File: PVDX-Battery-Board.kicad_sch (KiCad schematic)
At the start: 0 parts

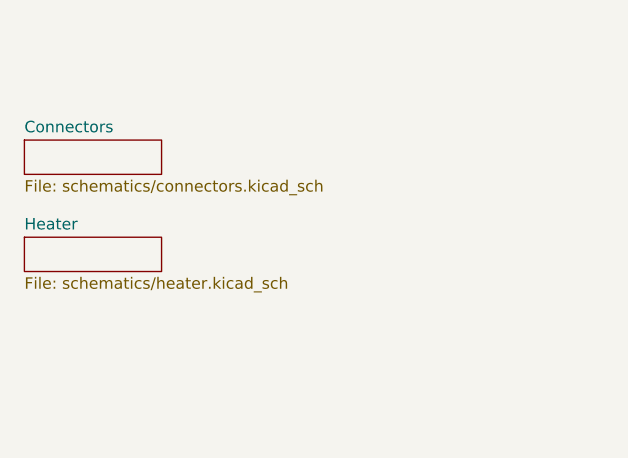
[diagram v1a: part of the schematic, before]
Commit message: Add battery overdischarge & short protections to board
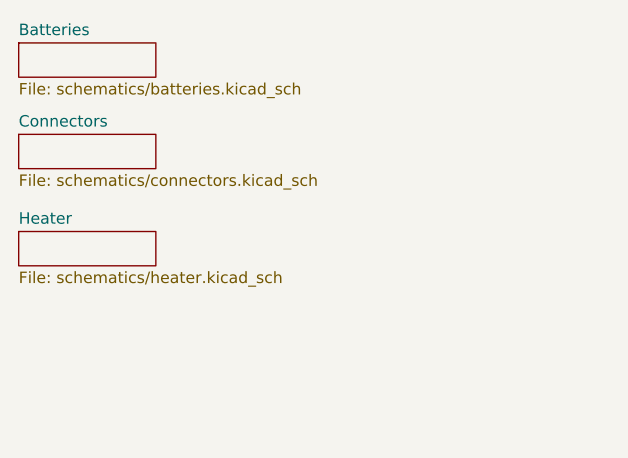
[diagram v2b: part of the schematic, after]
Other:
- added sheet Batteries (schematics/batteries.kicad_sch)
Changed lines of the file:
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@@
 	)
 	(sheet
-		(at 47.625 58.42)
+		(at 46.99 36.83)
+		(size 15.24 3.81)
+		(exclude_from_sim no)
+		(in_bom yes)
+		(on_board yes)
+		(dnp no)
+		(fields_autoplaced yes)
+		(stroke
+			(width 0.1524)
+			(type solid)
+		)
+		(fill
+			(color 0 0 0 0)
+		)
+		(property "Sheetname" "Batteries"
+			(at 46.99 36.1184 0)
+			(show_name no)
+			(do_not_autoplace no)
+			(effects
+				(font
+					(size 1.27 1.27)
+				)
+				(justify left bottom)
+			)
+		)
+		(property "Sheetfile" "schematics/batteries.kicad_sch"
+			(at 46.99 41.2246 0)
+			(show_name no)
+			(do_not_autoplace no)
+			(effects
+				(font
+					(size 1.27 1.27)
+				)
+				(justify left top)
+			)
+		)
+		(instances
+			(project "PVDX-Battery-Board"
+				(path "/c318761a-e6d3-4e59-aaa2-0d170bce7cde"
+					(page "4")
+				)
+			)
+		)
+	)
+	(sheet
+		(at 46.99 57.785)
 		(size 15.24 3.81)
 		(exclude_from_sim no)
@@
 		)
 		(property "Sheetname" "Heater"
-			(at 47.625 57.7084 0)
+			(at 46.99 57.0734 0)
 			(show_name no)
 			(do_not_autoplace no)
@@
 		)
 		(property "Sheetfile" "schematics/heater.kicad_sch"
-			(at 47.625 62.8146 0)
+			(at 46.99 62.1796 0)
 			(show_name no)
 			(do_not_autoplace no)
@@
 	)
 	(sheet
-		(at 47.625 47.625)
+		(at 46.99 46.99)
 		(size 15.24 3.81)
 		(exclude_from_sim no)
@@
 		)
 		(property "Sheetname" "Connectors"
-			(at 47.625 46.9134 0)
+			(at 46.99 46.2784 0)
 			(show_name no)
 			(do_not_autoplace no)
@@
 		)
 		(property "Sheetfile" "schematics/connectors.kicad_sch"
-			(at 47.625 52.0196 0)
+			(at 46.99 51.3846 0)
 			(show_name no)
 			(do_not_autoplace no)
